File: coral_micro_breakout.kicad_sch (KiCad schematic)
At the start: 3 parts, among them J1 Conn_01x03_Socket

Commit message: working on board
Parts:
- added D1: LED, LED_SMD:LED_0805_2012Metric_Pad1.15x1.40mm_HandSolder, symbol Device:LED
- added R1: 1.5k, Resistor_SMD:R_0805_2012Metric_Pad1.20x1.40mm_HandSolder, symbol Device:R
- C1: value 10uF -> 0.1uF; footprint (none) -> Capacitor_SMD:C_0504_1310Metric_Pad0.83x1.28mm_HandSolder
- J1: footprint (none) -> Connector_PinHeader_2.54mm:PinHeader_1x03_P2.54mm_Vertical
- U1: footprint (none) -> 00_parts_lib:coral_micro_board_mating
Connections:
- net +1.8VDC_RGB: now also U1.14 (1.8V); no longer U1. (VSYS)
- net +1.8VDC_TOF: now also U1.2 (1.8V); no longer U1. (VSYS)
- net +3.3VDC: now also U1.3 (3.3V); no longer U1. (VSYS)
- net +5VDC: now also C1.2, U1.24 (VSYS), R1.1; no longer C1.1, U1. (VSYS)
- net DEBUG_RX: now also J1.3 (Pin_3), U1.18 (UART6_RX); no longer J1.2 (Pin_2), U1. (VSYS)
- net DEBUG_TX: now also J1.2 (Pin_2), U1.17 (UART6_TX); no longer J1.3 (Pin_3), U1. (VSYS)
- net GND: now also C1.1, U1.1 (GND), U1.13 (GND), D1.1 (K); no longer C1.2, U1. (VSYS)
- net PWM_0: now also U1.22 (PWM_A); no longer U1. (VSYS)
- net PWM_1: now also U1.21 (PWM_B); no longer U1. (VSYS)
- net SCL: now also U1.11 (I2C1_SCL); no longer U1. (VSYS)
- net SDA: now also U1.12 (I2C1_SDA); no longer U1. (VSYS)
- new net: D1.2 (A), R1.2
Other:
- note added: "5V: R = (5V-1.8)/(2mA) = 1.5kOhm"
- note added: "Design note: TOF board already includes C and R. So none included here."
- moved on the sheet: J1

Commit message: made board
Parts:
- added R1, R3, R4, R5: 0, Resistor_SMD:R_0805_2012Metric_Pad1.20x1.40mm_HandSolder, symbol Device:R
- renumbered R1 to R2
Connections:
- net +1.8VDC_RGB: now also R3.1; no longer U1.14 (1.8V)
- net +1.8VDC_TOF: now also R4.2; no longer U1.2 (1.8V)
- net +3.3VDC: now also R5.2; no longer U1.3 (3.3V)
- net +5VDC: now also R1.1; no longer C1.2, R2.1, U1.24 (VSYS)
- new net: C1.2, R1.2, R2.1, U1.24 (VSYS)
- new net: R3.2, U1.14 (1.8V)
- new net: R4.1, U1.2 (1.8V)
- new net: R5.1, U1.3 (3.3V)
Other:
- note added: "0 Ohm R added for current testing."
- note added: "Coral Micro Breakout"

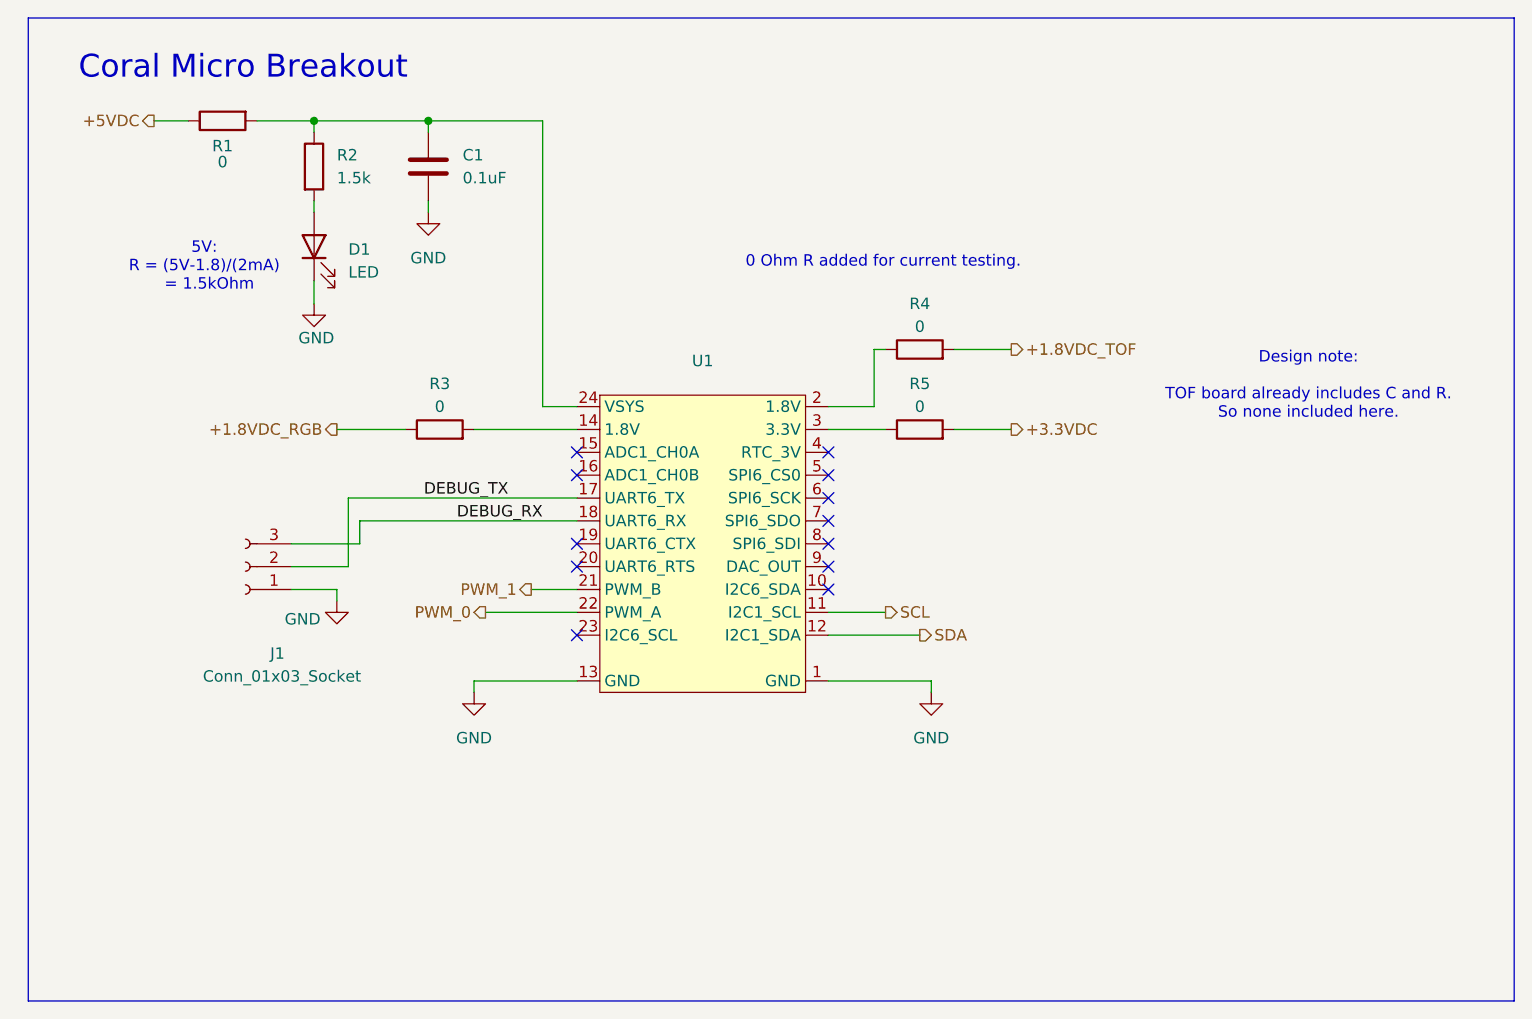
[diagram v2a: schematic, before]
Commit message: not working, reverting to old design
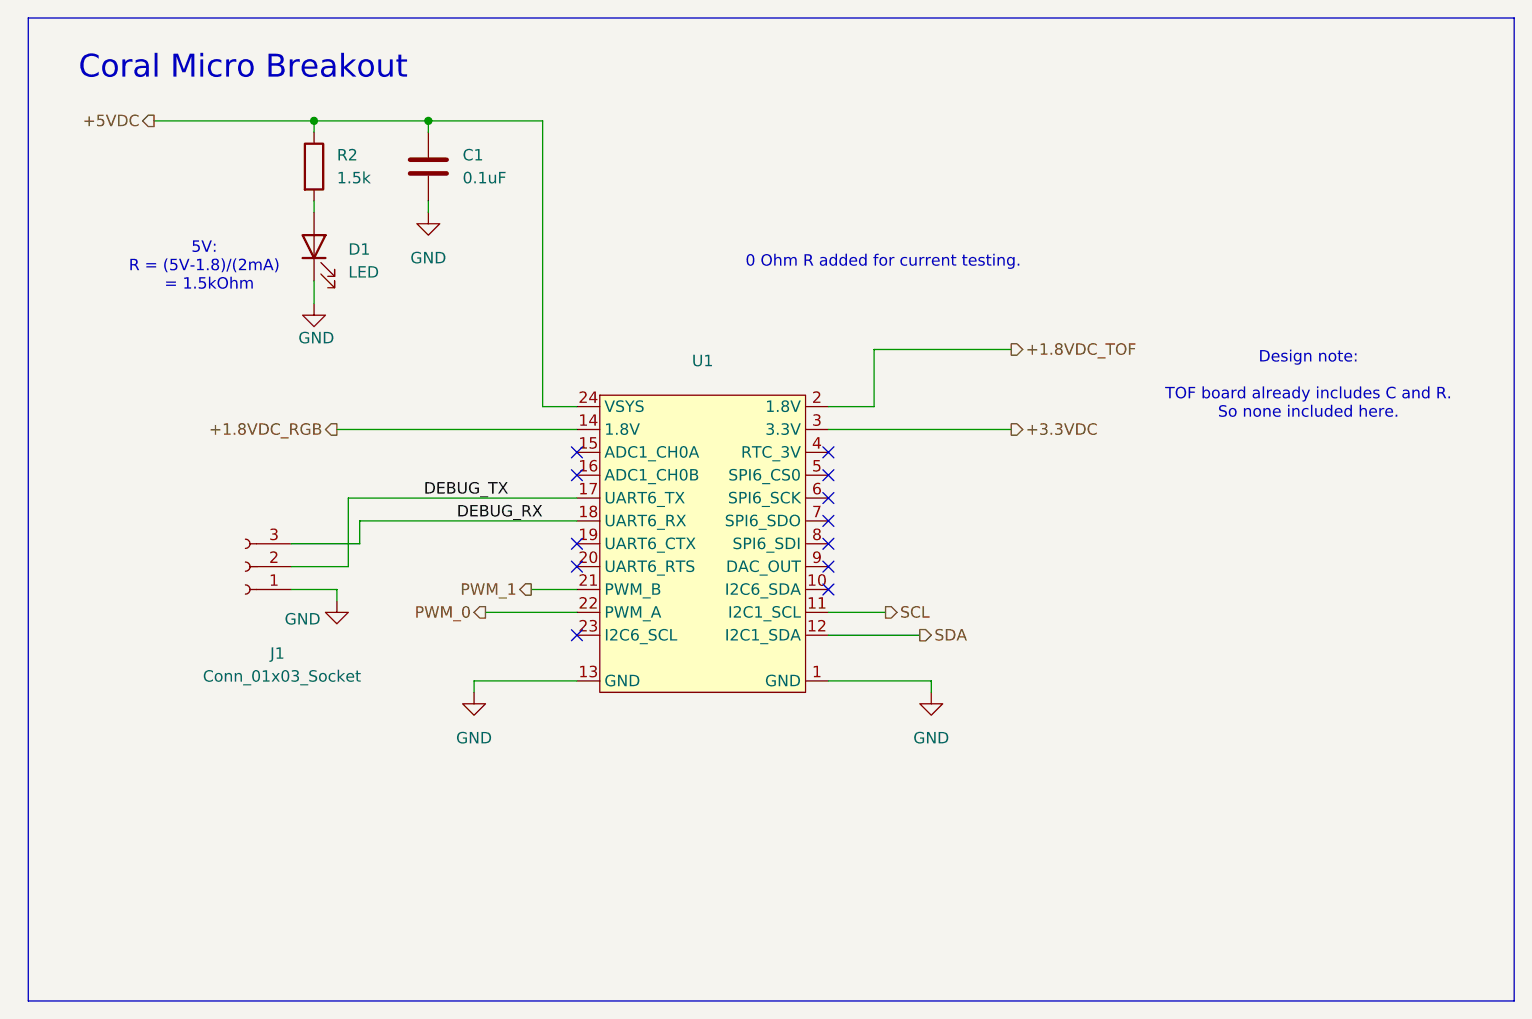
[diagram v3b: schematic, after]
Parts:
- removed R1, R3, R4, R5: 0, Resistor_SMD:R_0805_2012Metric_Pad1.20x1.40mm_HandSolder, symbol Device:R
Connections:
- net +1.8VDC_RGB: now also U1.14 (1.8V)
- net +1.8VDC_TOF: now also U1.2 (1.8V)
- net +3.3VDC: now also U1.3 (3.3V)
- net +5VDC: now also C1.2, R2.1, U1.24 (VSYS)

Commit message: latest updates, up to v2
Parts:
- renumbered R2 to R1
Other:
- note removed: "0 Ohm R added for current testing."
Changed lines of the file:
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@@
-		)
-	)
-	(text "0 Ohm R added for current testing."
-		(exclude_from_sim no)
-		(at 138.176 52.578 0)
-		(effects
-			(font
-				(size 1.27 1.27)
-			)
 		)
 	)
@@
 		(dnp no)
 		(fields_autoplaced yes)
-		(property "Reference" "R2"
+		(property "Reference" "R1"
 			(at 77.47 40.6399 0)
 			(effects
@@
 			(project "edge_human_detection_board"
 				(path "/f7edb1cc-a42a-4cc0-9a6f-d9bd2b944353/72abfcf8-e097-478e-98cf-ce55e9cba7c4"
-					(reference "R2")
+					(reference "R1")
 					(unit 1)
 				)
